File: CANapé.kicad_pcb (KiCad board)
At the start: 4 copper layers, 55.5 x 30.7 mm, 39 parts, among them J1 USB_C_Receptacle_USB2.0, J2 DB9_Male_MountingHoles, SW2 120, SW3 BOOT, SW4 RST, U1 NCP1117-3.3_SOT223, U2 SN65HVD232, U3 STM32F302C6Tx, Y1 8MHz

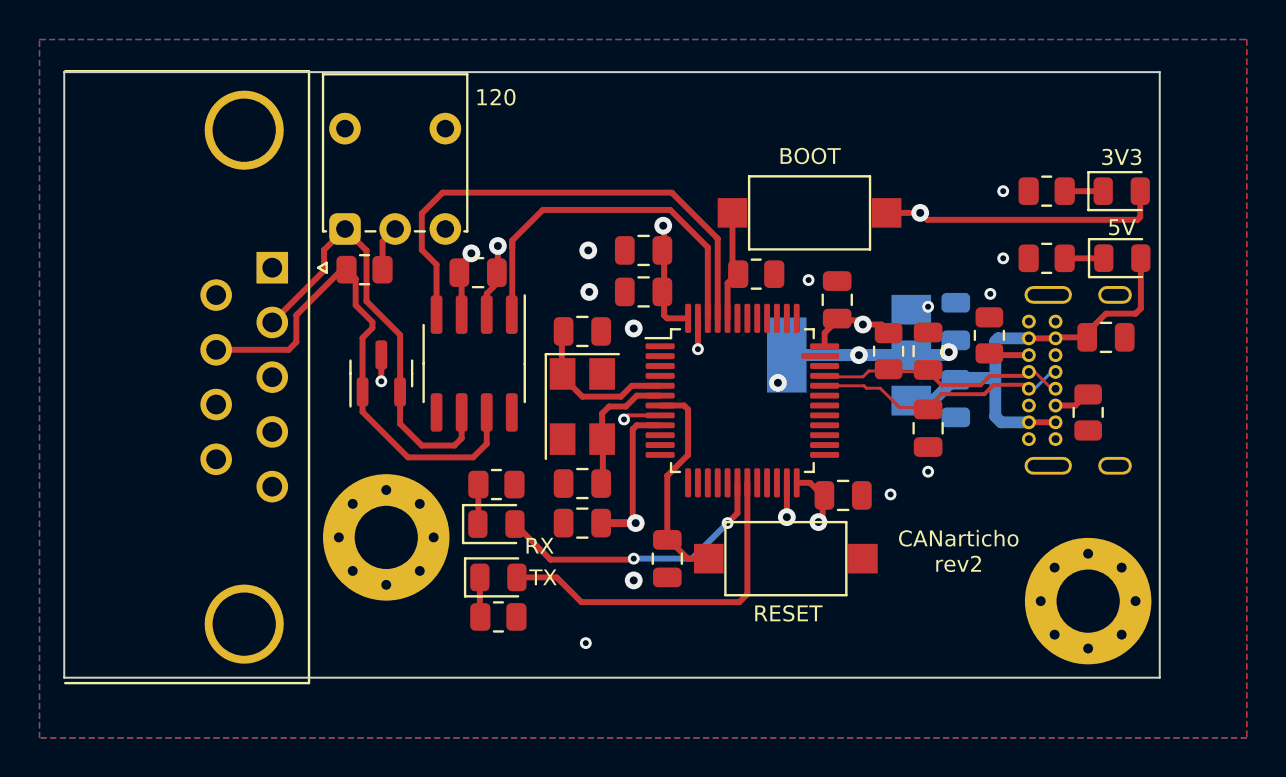
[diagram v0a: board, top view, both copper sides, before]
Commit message: v2 with db9 connector
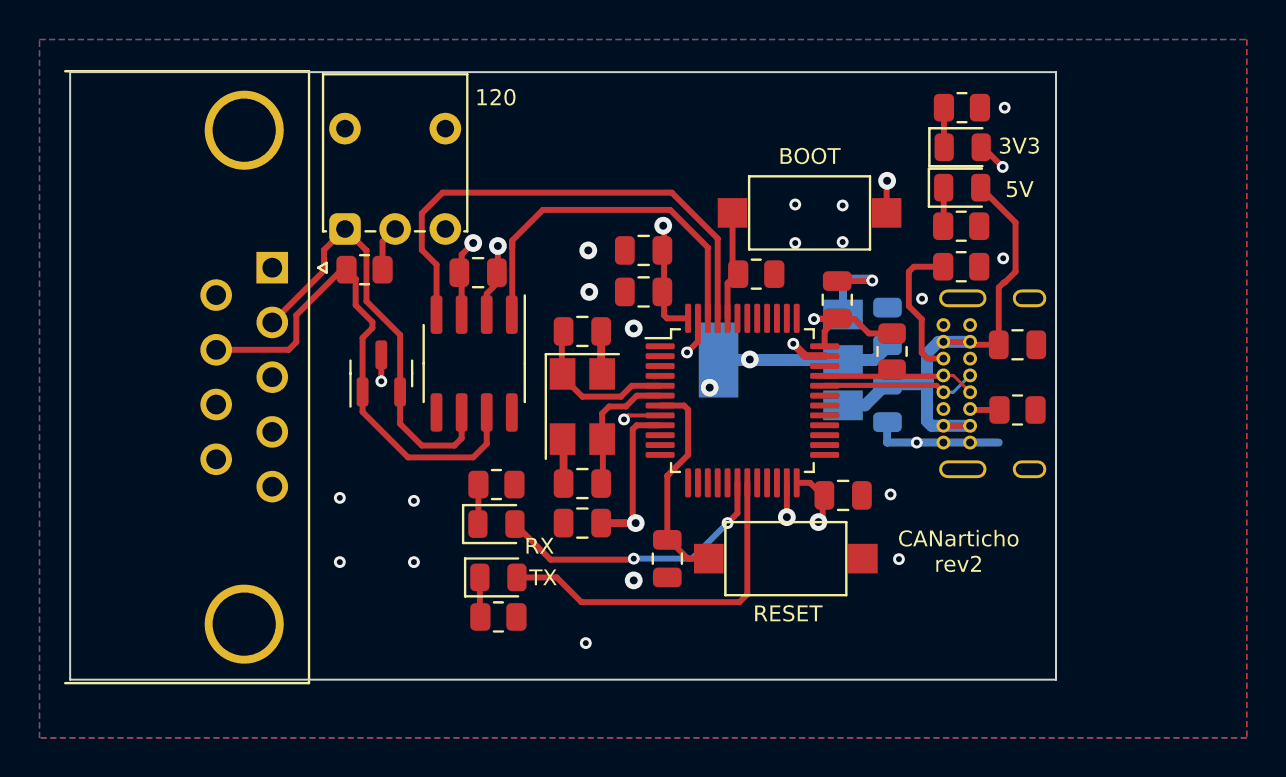
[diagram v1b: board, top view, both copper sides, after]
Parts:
- removed C3, C5: 47p, Capacitor_SMD:C_0805_2012Metric
- removed REF** (x2): MountingHole_3.2mm_M3_Pad_Via, MountingHole:MountingHole_3.2mm_M3_Pad_Via
- moved D2 8.85 mm to (174.8, 73.4)
- moved D1 8.35 mm to (174.8, 71.3)
- moved R4 6.02 mm to (174.8, 69.3), turned to 180 degrees
- moved R5 4.62 mm to (174.8, 75.3), turned to 180 degrees
- moved C6 4.49 mm to (177.6, 81.3)
- moved J1 4.33 mm to (173.8, 80.3)
- moved R2 3.76 mm to (174.8, 77.4), turned to 0 degrees
- moved R3 3.58 mm to (177.6, 84.7), turned to 0 degrees
- moved C2 3.46 mm to (171.0, 80.4)
- moved U1 3.46 mm to (165.6, 82.1)
- moved C1 3.46 mm to (171.0, 84.3)
- moved R7 0.18 mm to (171.2, 81.7)
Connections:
- J1 pad S1: GND -> unconnected-(J1-PadS1)
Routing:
- net GND: track 11.3 -> 28.6 mm, vias 17 -> 26
- net +3V3: track 47.7 -> 41.8 mm
- net Net-(J1-PadA5): track 2.00 -> 7.43 mm
- net /USB-: track 13.1 -> 7.93 mm
- net /USB+: track 12.8 -> 7.98 mm
- net +5V: track 22.5 -> 26.4 mm
- removed copper zone on In1.Cu, net +5V
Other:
- board size 55.5 x 30.7 mm -> 49.9 x 30.8 mm
